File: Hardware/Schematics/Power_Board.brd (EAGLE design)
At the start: 139.3 x 49 mm, 83 parts, among them J1 1X2-3.5MM, J2 1X2-3.5MM, J3 1X2-3.5MM, J4 1X2-3.5MM, Q5 4.096MHz, Q8 4.096MHz, Q9 4.096MHz

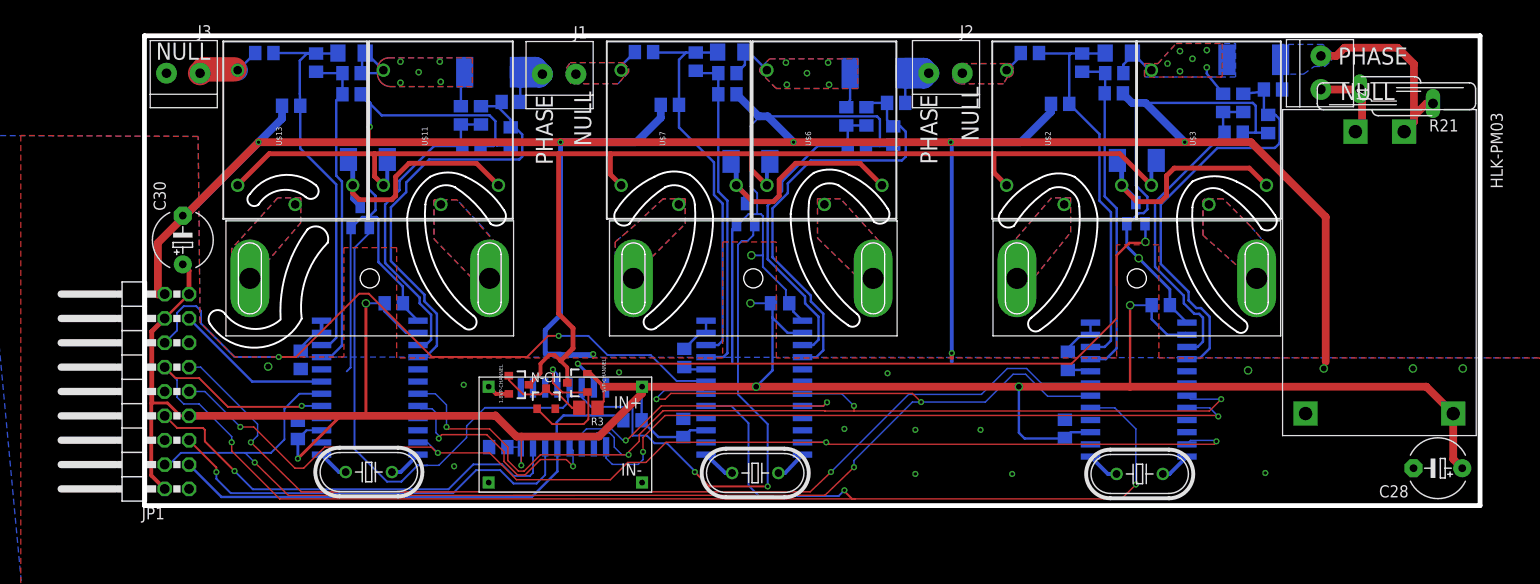
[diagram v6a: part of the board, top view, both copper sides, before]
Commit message: Updated board versions to final (v1) version, and added renders.
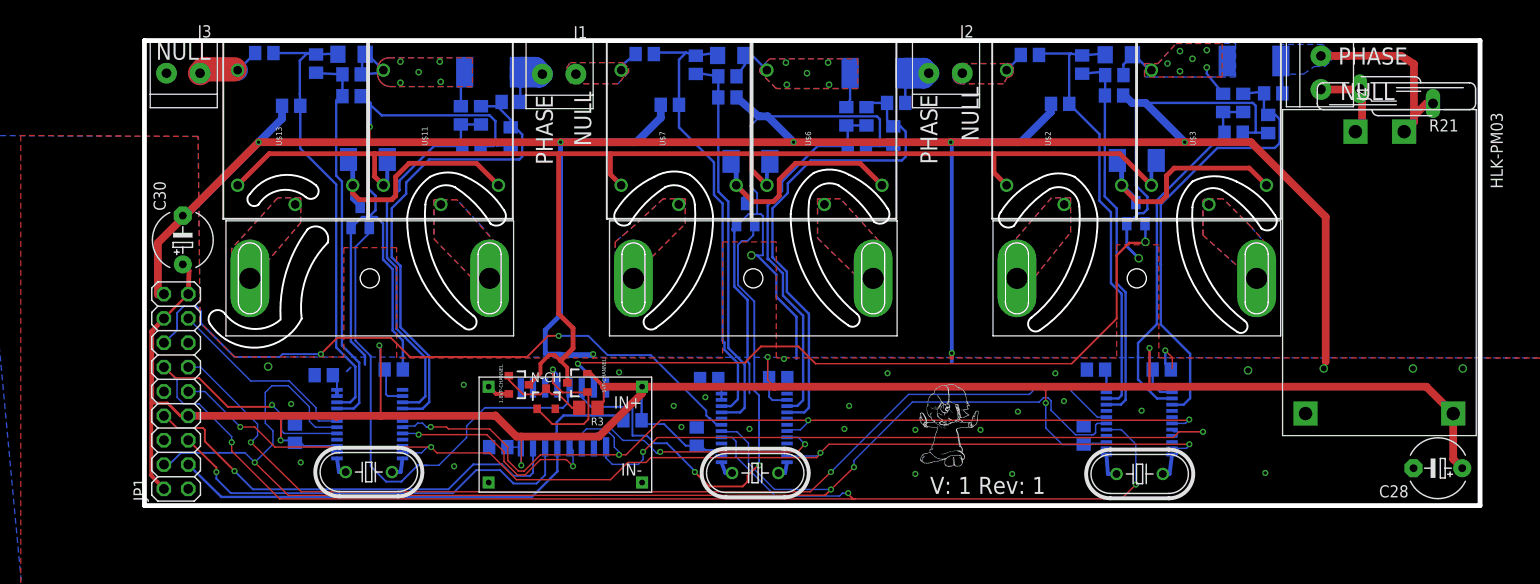
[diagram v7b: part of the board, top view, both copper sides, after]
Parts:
- JP1: device pinhead:2X09/90 -> pinhead:2X09
- U$14, U$8, U$9: device PowerSocket:SO24L -> PowerSocket:SSOP24
- moved C3 7.80 mm to (76.8, 13.3)
- moved C21 6.90 mm to (36.7, 14.2)
- moved C9 6.71 mm to (116.8, 14.2)
- moved JP1 5.00 mm to (14.0, 11.9)
- moved U$8 4.20 mm to (74.3, 8.10)
- moved U$14 3.80 mm to (34.2, 8.50)
- moved C1 3.41 mm to (69.6, 13.2), turned to 0 degrees
- moved U$9 3.20 mm to (114.5, 8.90)
- moved C8 3.08 mm to (109.9, 14.2), turned to 0 degrees
- moved C19 2.88 mm to (29.4, 13.6), turned to 0 degrees
- moved C10 2.07 mm to (108.7, 7.31)
- moved C2 1.66 mm to (68.3, 7.20)
- moved C20 0.50 mm to (26.4, 7.50)
- moved R9 0.41 mm to (128.4, 43.0)
- moved R7 0.36 mm to (71.9, 46.9)
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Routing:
- net VCC: track 293.3 -> 266.3 mm, vias 7 -> 6
- net RESET: track 109.6 -> 98.0 mm
- net SDO: track 152.0 -> 142.5 mm, vias 4 -> 3
- net VIN+3: track 41.1 -> 48.5 mm
- net VIN+2: track 40.9 -> 48.2 mm
- net VIN-3: track 34.4 -> 40.9 mm
- net N$13: track 33.3 -> 39.7 mm
- net VIN-2: track 34.5 -> 40.7 mm
- net N$24: track 44.5 -> 50.4 mm
- net N$4: track 34.4 -> 40.1 mm
- net VIN+1: track 41.2 -> 46.8 mm
- net N$7: track 45.6 -> 51.0 mm
- net SCLK: track 163.1 -> 157.8 mm
- net N$42: track 33.3 -> 38.5 mm
- net VIN-1: track 34.9 -> 39.6 mm
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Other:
- board size 139.3 x 49 mm -> 139.3 x 48.5 mm
- board text added: "V: 1 Rev: 1"
